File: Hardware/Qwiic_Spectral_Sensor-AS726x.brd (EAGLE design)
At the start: 25.4 x 25.4 mm, 32 parts, among them J2 Serial Interface, J5 Flash Programming, U1 AS726X, U3 4MB Flash

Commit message: Updated LED
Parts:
- removed U$1: (no value), SparkFun-Aesthetics:SFE_LOGO_FLAME_.2
- removed U$3: (no value), SparkFun-Aesthetics:SFE_LOGO_FLAME_.1
- removed U$4: (no value), SparkFun-Aesthetics:SFE_LOGO_FLAME_.3
- added LOGO2: SFE_LOGO_FLAME.2_INCH, SparkFun-Aesthetics:SFE_LOGO_FLAME_.2
- D2: value 5700k -> White, 60mA; device SparkX:SUPER_BRIGHT_SMD_LED_1206 -> SparkFun-LED:SUPER_BRIGHT_SMD_LED_3014
- LOGO1: value SFE_LOGO_NAME_FLAME.1_INCH -> SFE_LOGO_FLAME.2_INCH; device SparkFun-Aesthetics:SFE_LOGO_NAME_FLAME_.1 -> SparkFun-Aesthetics:SFE_LOGO_FLAME_.2
- moved LOGO1 64.5 mm to (21.0, 1.27)
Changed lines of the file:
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@@
 <layer number="22" name="bPlace" color="14" fill="1" visible="yes" active="yes"/>
 <layer number="23" name="tOrigins" color="15" fill="1" visible="yes" active="yes"/>
-<layer number="24" name="bOrigins" color="15" fill="1" visible="no" active="yes"/>
+<layer number="24" name="bOrigins" color="15" fill="1" visible="yes" active="yes"/>
 <layer number="25" name="tNames" color="7" fill="1" visible="no" active="yes"/>
 <layer number="26" name="bNames" color="7" fill="1" visible="no" active="yes"/>
@@
 <layer number="230" name="230bmp" color="7" fill="1" visible="no" active="yes"/>
 <layer number="231" name="231bmp" color="7" fill="1" visible="no" active="yes"/>
+<layer number="232" name="Eagle3D_PG2" color="7" fill="1" visible="yes" active="yes"/>
+<layer number="233" name="Eagle3D_PG3" color="7" fill="1" visible="yes" active="yes"/>
 <layer number="248" name="Housing" color="7" fill="1" visible="no" active="yes"/>
 <layer number="249" name="Edge" color="7" fill="1" visible="no" active="yes"/>
@@
 </element>
 <element name="J4" library="SparkX" package="1X04_1MM_RA" value="" x="20.32" y="12.7" rot="R90"/>
-<element name="D2" library="SparkX" package="SUPER_BRIGHT_SMD_LED_1206" value="5700k" x="16.891" y="12.7" smashed="yes" rot="R90"/>
+<element name="D2" library="SparkFun-LED" package="SUPER_BRIGHT_SMD_LED_3014" value="White, 60mA" x="16.891" y="12.7" smashed="yes" rot="R90">
+<attribute name="VALUE" value="White, 60mA" x="16.891" y="12.7" size="1.778" layer="27" rot="R90" display="off"/>
+<attribute name="PROD_ID" value="DIO-13728" x="16.891" y="12.7" size="1.778" layer="27" rot="R90" display="off"/>
+</element>
 <element name="J5" library="SparkFun-Connectors" package="2X3_TEST_POINTS" value="Flash Programming" x="12.7" y="19.05" rot="MR270"/>
 <element name="D4" library="SparkX" package="LED_5MM_NOSILK" value="Incandescent" x="22.225" y="17.272" rot="MR0"/>
 <element name="JP4" library="SparkFun-Jumpers" package="SMT-JUMPER_2_NC_PASTE_NO-SILK" value="" x="16.891" y="9.779" rot="R270"/>
-<element name="U$1" library="SparkFun-Aesthetics" package="SFE_LOGO_FLAME_.2" value="" x="20.32" y="1.27"/>
 <element name="U$2" library="SparkFun-Aesthetics" package="REVISION" value="" x="-2.54" y="-24.13"/>
-<element name="U$3" library="SparkFun-Aesthetics" package="SFE_LOGO_FLAME_.1" value="" x="21.717" y="2.667"/>
-<element name="U$4" library="SparkFun-Aesthetics" package="SFE_LOGO_FLAME_.3" value="" x="25.273" y="1.27" rot="MR0"/>
-<element name="LOGO1" library="SparkFun-Aesthetics" package="SFE_LOGO_NAME_FLAME_.1" value="SFE_LOGO_NAME_FLAME.1_INCH" x="-35.179" y="-30.48"/>
+<element name="LOGO1" library="SparkFun-Aesthetics" package="SFE_LOGO_FLAME_.2" value="SFE_LOGO_FLAME.2_INCH" x="20.955" y="1.27"/>
+<element name="LOGO2" library="SparkFun-Aesthetics" package="SFE_LOGO_FLAME_.2" value="SFE_LOGO_FLAME.2_INCH" x="25.019" y="1.27" rot="MR0"/>
 </elements>
 <signals>

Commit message: Added LED, I2C connectors to SFE library and changed components in schematic
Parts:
- J1, J4: value (none) -> Qwiic Right Angle; device SparkX:1X04_1MM_RA -> SparkFun-Connectors:1X04_1MM_RA
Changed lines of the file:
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@@
 <layer number="23" name="tOrigins" color="15" fill="1" visible="yes" active="yes"/>
 <layer number="24" name="bOrigins" color="15" fill="1" visible="yes" active="yes"/>
-<layer number="25" name="tNames" color="7" fill="1" visible="no" active="yes"/>
+<layer number="25" name="tNames" color="7" fill="1" visible="yes" active="yes"/>
 <layer number="26" name="bNames" color="7" fill="1" visible="no" active="yes"/>
 <layer number="27" name="tValues" color="7" fill="1" visible="no" active="yes"/>
@@
 <attribute name="PROD_ID" value="CAP-00868" x="7.62" y="19.05" size="1.778" layer="27" font="vector" ratio="15" rot="R90" display="off"/>
 </element>
-<element name="J1" library="SparkX" package="1X04_1MM_RA" value="" x="5.08" y="12.7" rot="R270"/>
+<element name="J1" library="SparkFun-Connectors" package="1X04_1MM_RA" value="Qwiic Right Angle" x="5.08" y="12.7" rot="R270">
+<attribute name="PROD_ID" value="CONN-13729" x="5.08" y="12.7" size="1.778" layer="27" rot="R270" display="off"/>
+<attribute name="VALUE" value="Qwiic Right Angle" x="5.08" y="12.7" size="1.778" layer="27" rot="R270" display="off"/>
+</element>
 <element name="D1" library="SparkFun-LED" package="LED-0603" value="BLUE" x="18.669" y="12.7" smashed="yes" rot="R90">
 <attribute name="PROD_ID" value="DIO-08575" x="18.669" y="12.7" size="1.778" layer="27" font="vector" ratio="15" rot="R90" display="off"/>
@@
 <attribute name="NAME" x="14.478" y="22.479" size="0.6096" layer="25" font="vector" ratio="20" rot="R180"/>
 </element>
-<element name="J4" library="SparkX" package="1X04_1MM_RA" value="" x="20.32" y="12.7" rot="R90"/>
+<element name="J4" library="SparkFun-Connectors" package="1X04_1MM_RA" value="Qwiic Right Angle" x="20.32" y="12.7" rot="R90">
+<attribute name="PROD_ID" value="CONN-13729" x="20.32" y="12.7" size="1.778" layer="27" rot="R90" display="off"/>
+<attribute name="VALUE" value="Qwiic Right Angle" x="20.32" y="12.7" size="1.778" layer="27" rot="R90" display="off"/>
+</element>
 <element name="D2" library="SparkFun-LED" package="SUPER_BRIGHT_SMD_LED_3014" value="White, 60mA" x="16.891" y="12.7" smashed="yes" rot="R90">
 <attribute name="VALUE" value="White, 60mA" x="16.891" y="12.7" size="1.778" layer="27" rot="R90" display="off"/>

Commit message: Updated all schematics to point to proper library
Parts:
- U1: value AS726X -> IR; device SparkX:LGA20 -> SparkFun-Sensors:LGA20
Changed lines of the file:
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@@
 <element name="FD1" library="SparkFun-Aesthetics" package="FIDUCIAL-1X2" value="FIDUCIAL1X2" x="1.27" y="1.27"/>
 <element name="FD2" library="SparkFun-Aesthetics" package="FIDUCIAL-1X2" value="FIDUCIAL1X2" x="24.13" y="20.32"/>
-<element name="U1" library="SparkX" package="LGA20" value="AS726X" x="12.7" y="12.7" smashed="yes" rot="R270">
+<element name="U1" library="SparkFun-Sensors" package="LGA20" value="IR" x="12.7" y="12.7" smashed="yes" rot="R270">
 <attribute name="NAME" x="16.129" y="14.351" size="0.762" layer="25" rot="R270"/>
-<attribute name="VALUE" x="10.795" y="8.763" size="0.762" layer="27"/>
+<attribute name="VALUE" value="IR" x="10.795" y="8.763" size="0.762" layer="27"/>
+<attribute name="PROD_ID" value="IC-13731" x="12.7" y="12.7" size="1.778" layer="27" rot="R270" display="off"/>
 </element>
 <element name="R3" library="SparkFun-Resistors" package="0603" value="10k" x="7.62" y="13.97" rot="R90">

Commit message: Fixed minor borad layout issues
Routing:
- net !RST: track 25.5 -> 27.5 mm
- net MOSI: track 16.4 -> 14.6 mm
- net 3.3V: track 84.9 -> 86.4 mm
- net RX/SCL: track 51.0 -> 49.8 mm

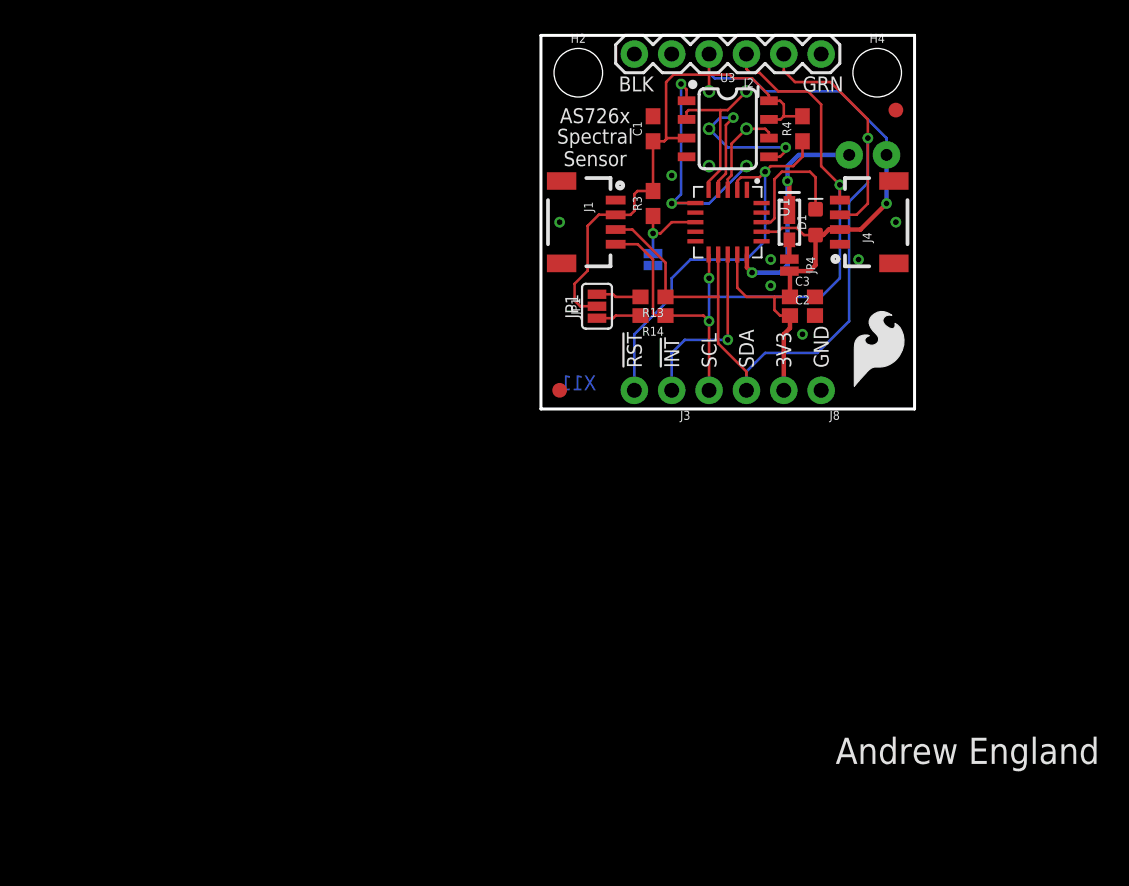
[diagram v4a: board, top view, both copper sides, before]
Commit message: Post design review changes. Cream on JP1 and AS726X still needs to be changed
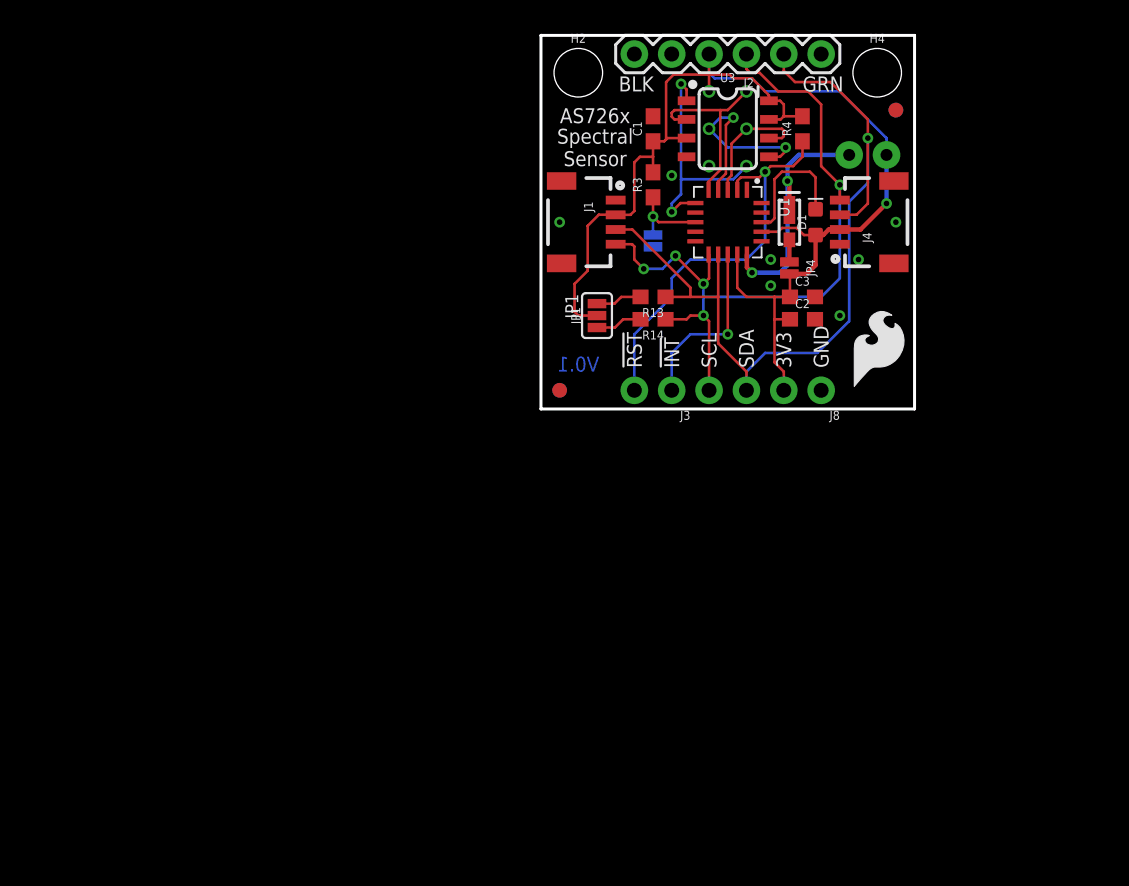
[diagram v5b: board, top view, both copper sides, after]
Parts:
- added FD3, FD4: FIDUCIAL1X2, SparkFun-Aesthetics:FIDUCIAL-1X2
- moved JP2 1.27 mm to (7.62, 11.4)
- moved R3 1.27 mm to (7.62, 15.2)
- moved JP1 0.64 mm to (3.81, 6.35)
- moved C2 0.25 mm to (17.8, 6.10)
- moved R14 0.25 mm to (7.62, 6.10)
- moved JP4 0.19 mm to (16.9, 9.59)
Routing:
- net SCK: track 6.69 -> 8.71 mm
- net MISO: track 10.9 -> 12.8 mm
- net 3.3V: track 86.4 -> 88.3 mm
- net RX/SCL: track 49.8 -> 50.9 mm, vias 3 -> 5
- net TX/SDA: track 59.1 -> 59.8 mm
- net !CS_EE: track 17.5 -> 16.9 mm
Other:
- board text added: "+"
- board text added: "-"
- board text added: "I2C-0x49"
- board text added: "V0.1"
- board text removed: "Bulb"
- board text removed: "I2C"
- board text removed: "X11"
